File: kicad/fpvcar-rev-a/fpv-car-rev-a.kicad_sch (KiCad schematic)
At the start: 13 parts, among them J1 CAMERA, U1 ESP32-S3-WROOM-1, U2 AMS1117-3.3

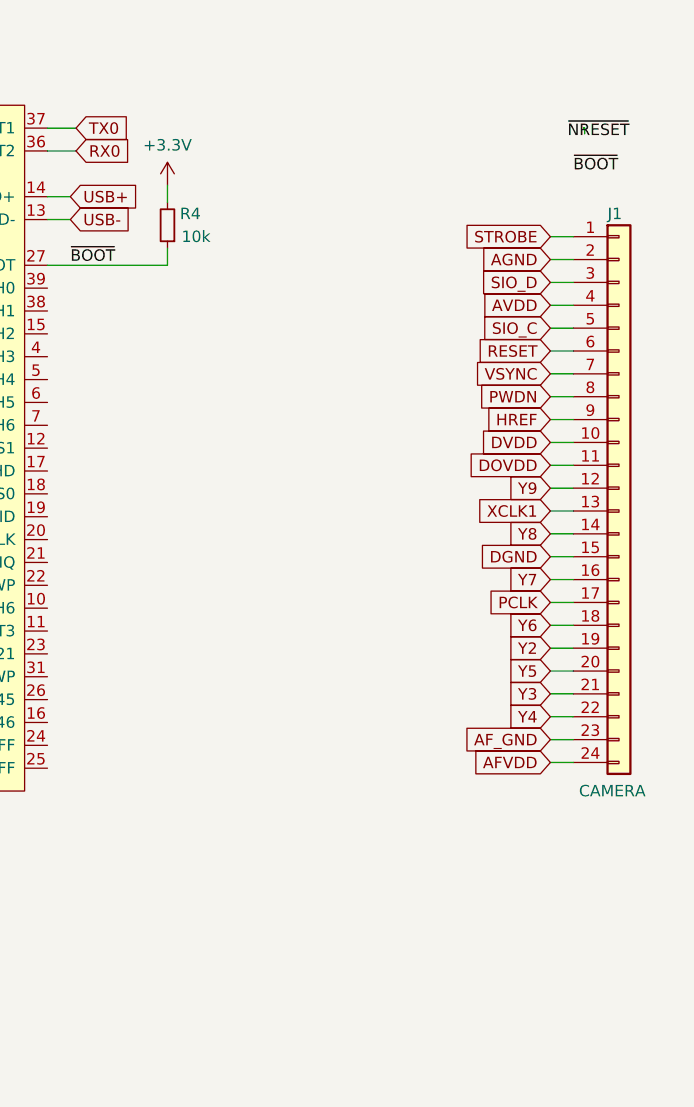
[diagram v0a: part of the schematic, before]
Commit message: Initial testcode (for esp32cam) and some more improvements on schematic
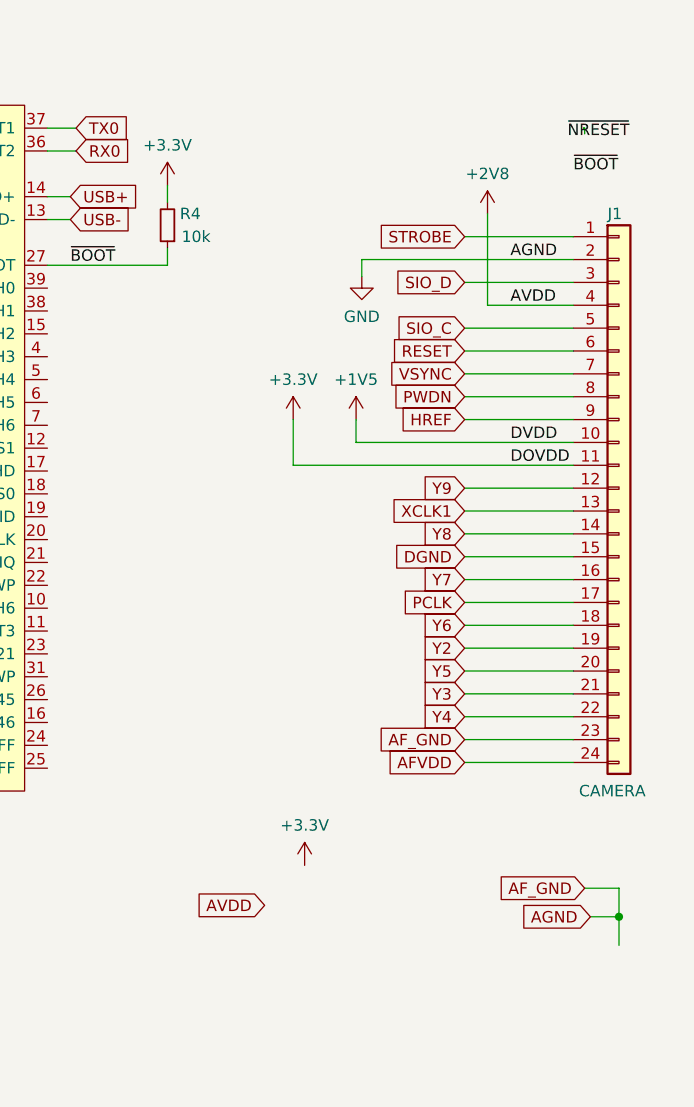
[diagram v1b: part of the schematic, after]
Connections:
- net AF_GND is gone; now on net GND: J1.23 (Pin_23)
- net AGND is gone; now on net GND: J1.2 (Pin_2)
- net DOVDD is gone; now on net +3.3V: J1.11 (Pin_11)
- net AVDD renamed +2V8
- net DVDD renamed +1V5

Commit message: Schematic progress!
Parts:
- added C10, C9: 47u, Capacitor_SMD:C_Elec_4x5.4, symbol Device:C_Small
- added C11: 2.2u, Capacitor_SMD:C_0402_1005Metric, symbol Device:C_Small
- added C12: 10n, Capacitor_SMD:C_0402_1005Metric, symbol Device:C_Small
- added C5, C6, C7, C8: 10u, symbol Device:C_Small
- added J2: Steering, symbol Connector_Generic:Conn_01x03
- added J3: RGB Leds, symbol Connector_Generic:Conn_01x03
- added J4: Battery, symbol Connector_Generic:Conn_01x02
- added J5: Debug UART, symbol Connector_Generic:Conn_01x03
- added J6, J7: M1, symbol Connector_Generic:Conn_01x02
- added J8: NRF24L01, Connector_PinSocket_2.54mm:PinSocket_1x08_P2.54mm_Vertical, symbol Connector_Generic:Conn_01x08
- added OSC1: YF4024M00033001, easyeda2kicad:OSC-SMD_4P-L3.2-W2.5-BL_1C210000BB0F, symbol easyeda2kicad:YF4024M00033001
- added R5: 10k, symbol Device:R_Small
- added SW1, SW2: SW_SPST, symbol Switch:SW_SPST
- added TP1: TestPoint, symbol Connector:TestPoint
- added U3: TLV74328PDBVR, easyeda2kicad:SOT-23-5_L3.0-W1.7-P0.95-LS2.8-BL, symbol easyeda2kicad:TLV74328PDBVR
- added U4: TLV74315PDBVR, easyeda2kicad:SOT-23-5_L2.9-W1.6-P0.95-LS2.8-BL, symbol easyeda2kicad:TLV74315PDBVR
- added U5: DRV8833PWP, Package_SO:HTSSOP-16-1EP_4.4x5mm_P0.65mm_EP3.4x5mm_Mask2.46x2.31mm_ThermalVias, symbol Driver_Motor:DRV8833PWP
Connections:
- net +1V5: now also C8.1, U4.5 (OUT)
- net +2V8: now also C5.1, U3.5 (OUT)
- net +3.3V: now also C10.1, J8.1 (Pin_1), OSC1.4 (VDD)
- net GND: now also C10.2, C11.1, C5.2, C6.2, C7.2, C8.2, C9.2, J2.3 (Pin_3), J3.3 (Pin_3), J4.2 (Pin_2), J5.3 (Pin_3), J8.2 (Pin_2), OSC1.2 (GND), SW1.2 (B), SW2.2 (B), U3.2 (GND), U4.2 (GND), U5.13 (GND), U5.17 (GND(PPAD)), U5.3 (AISEN), U5.6 (BISEN); no longer J1.23 (Pin_23)
- net RX0: now also J5.2 (Pin_2)
- net TX0: now also J5.1 (Pin_1)
- net VBUS: now also C6.1, C7.1, U3.1 (IN), U3.3 (EN), U4.1 (IN), U4.3 (EN)
- net XCLK1: now also OSC1.3 (OUT)
- net ~{BOOT}: now also SW1.1 (A)
- net ~{NRESET}: now also SW2.1 (A)
- new net: R5.2, U5.1 (nSLEEP)
- new net: C12.2, U5.11 (VCP)
- new net: C11.2, U5.14 (VINT)
- new net +5V: J2.2 (Pin_2), J3.2 (Pin_2)
- new net AF_GND: J1.23 (Pin_23)
- new net MOTOR_1_IN: J6.1 (Pin_1), U5.2 (AOUT1)
- new net MOTOR_1_OUT: J6.2 (Pin_2), U5.4 (AOUT2)
- new net MOTOR_2_IN: J7.1 (Pin_1), U5.7 (BOUT1)
- new net MOTOR_2_OUT: J7.2 (Pin_2), U5.5 (BOUT2)
- new net MOTOR_A_IN1: U5.16 (AIN1)
- new net MOTOR_A_IN2: U5.15 (AIN2)
- new net MOTOR_B_IN1: U5.9 (BIN1)
- new net MOTOR_B_IN2: U5.10 (BIN2)
- new net NRF_CE: J8.3 (Pin_3)
- new net NRF_CSN: J8.4 (Pin_4)
- new net NRF_IRQ: J8.8 (Pin_8)
- new net NRF_MISO: J8.7 (Pin_7)
- new net NRF_MOSI: J8.6 (Pin_6)
- new net NRF_SCK: J8.5 (Pin_5)
- new net RGB_LED: J3.1 (Pin_1)
- new net STEER: J2.1 (Pin_1)
- new net VBAT: J4.1 (Pin_1)
- new net VCC: C12.1, C9.1, R5.1, U5.12 (VM)
- new net ~{MOTOR_NFAULT}: TP1.1, U5.8 (nFAULT)
- no-connect marks 0 -> 3
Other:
- note added: "Buttons"
- note added: "Camera (OV5640)"
- note added: "Connectors"
- note added: "LEDs"
- note added: "MCU"
- note added: "Motor driver (H-bridge)"
- note added: "NRF24L01 Radio (smd module)"
- note added: "Oscillator for camera"
- note added: "Power supplies"
- moved on the sheet: C1, C2, C3, C4, D1, D2, J1, R1, R2, R3, R4, U1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

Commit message: More schematic improvements
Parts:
- removed OSC1: YF4024M00033001, easyeda2kicad:OSC-SMD_4P-L3.2-W2.5-BL_1C210000BB0F, symbol easyeda2kicad:YF4024M00033001
- added J10, J9: GPIO, symbol Connector_Generic:Conn_01x04
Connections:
- net +3.3V: now also J10.3 (Pin_3)
- net +5V: now also J9.3 (Pin_3)
- net GND: now also J10.4 (Pin_4), J9.4 (Pin_4)
- net RESET renamed ~{RESET}
- new net GPIO00: J10.1 (Pin_1), J10.2 (Pin_2), J9.1 (Pin_1), J9.2 (Pin_2)
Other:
- note added: "- RESET: Active low, internal pull-up - PWDN (Power down): Active high, internal pull-down"
- note added: "Pinouts - SIOC - SCCB Input clock - SIOD - SCCB Data - XCLK1 - System input clock - VSYNC - DVP VSYNC output - HREF - DVP HREF output Input clock to camera is driven by GPIOs on ESP"
- note removed: "Oscillator for camera"
- moved on the sheet: C1, C11, C12, C2, C5, C6, C7, C8, C9, D1, D2, R1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

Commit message: Swapped to OV2640 camera, started layout
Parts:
- removed C7, C8: 10u, symbol Device:C_Small
- removed J3: RGB Leds, symbol Connector_Generic:Conn_01x03
- removed U2: AMS1117-3.3, Package_TO_SOT_SMD:SOT-223-3_TabPin2, symbol Regulator_Linear:AMS1117-3.3
- removed U3: TLV74328PDBVR, easyeda2kicad:SOT-23-5_L3.0-W1.7-P0.95-LS2.8-BL, symbol easyeda2kicad:TLV74328PDBVR
- removed U4: TLV74315PDBVR, easyeda2kicad:SOT-23-5_L2.9-W1.6-P0.95-LS2.8-BL, symbol easyeda2kicad:TLV74315PDBVR
- added C13: 0.1u, Capacitor_SMD:C_0402_1005Metric, symbol Device:C_Small
- added C14, C15, C18, C19: 10u, Capacitor_SMD:C_0603_1608Metric, symbol Device:C_Small
- added D3: D_Schottky, Diode_SMD:D_SOD-123, symbol Device:D_Schottky
- added D4: Schottky, Diode_SMD:D_SOD-123, symbol Device:D_Schottky
- added H1, H2, H3, H4: MountingHole_Pad, symbol Mechanical:MountingHole_Pad
- added J11: USB C, easyeda2kicad:USB-SMD_GT-USB-7010AN, symbol Connector:USB_C_Receptacle_USB2.0
- added J12, J13: GPIO, Connector_PinSocket_2.54mm:PinSocket_1x04_P2.54mm_Vertical, symbol Connector_Generic:Conn_01x04
- added J14: RGB FL, Connector_PinSocket_2.00mm:PinSocket_1x04_P2.00mm_Vertical, symbol Connector_Generic:Conn_01x04
- added J15: RGB FR, Connector_PinSocket_2.00mm:PinSocket_1x04_P2.00mm_Vertical, symbol Connector_Generic:Conn_01x04
- added J16: RGB BL, Connector_PinSocket_2.00mm:PinSocket_1x04_P2.00mm_Vertical, symbol Connector_Generic:Conn_01x04
- added J17: RGB BR, Connector_PinSocket_2.00mm:PinSocket_1x04_P2.00mm_Vertical, symbol Connector_Generic:Conn_01x04
- added Q1: Q_PMOS_GSD, Package_TO_SOT_SMD:SOT-23, symbol Device:Q_PMOS_GSD
- added R10: 10k, Resistor_SMD:R_0402_1005Metric, symbol Device:R
- added R11, R13, R6, R7: 10k, Resistor_SMD:R_0402_1005Metric, symbol Device:R_Small
- added R12, R14: 4.7k, Resistor_SMD:R_0402_1005Metric, symbol Device:R_Small
- added R8, R9: 5.11k, Resistor_SMD:R_0402_1005Metric, symbol Device:R
- added U2: AMS1117-5.0, Package_TO_SOT_SMD:SOT-223-3_TabPin2, symbol Regulator_Linear:AMS1117-5.0
- added U3: XC6206-1.2V, Package_TO_SOT_SMD:SOT-23-3, symbol Regulator_Linear:XC6206PxxxMR
- added U4: XC6206-2.8V, Package_TO_SOT_SMD:SOT-23-3, symbol Regulator_Linear:XC6206PxxxMR
- added U6: WL2803K33-5/TR, Package_TO_SOT_SMD:SOT-89-5, symbol easyeda2kicad:WL2803K33-5_TR
- C1, C2, C3, C5, C6: footprint (none) -> Capacitor_SMD:C_0603_1608Metric
- C10, C9: footprint Capacitor_SMD:C_Elec_4x5.4 -> Capacitor_SMD:C_1206_3216Metric
- C4: footprint (none) -> Capacitor_SMD:C_0402_1005Metric
- D1, D2: footprint (none) -> LED_SMD:LED_0603_1608Metric
- J10, J9: footprint (none) -> Connector_PinSocket_2.54mm:PinSocket_1x04_P2.54mm_Vertical
- J2, J5: footprint (none) -> Connector_PinSocket_2.54mm:PinSocket_1x03_P2.54mm_Vertical
- J4, J6: footprint (none) -> Connector_PinSocket_2.54mm:PinSocket_1x02_P2.54mm_Vertical
- J7: value M1 -> M2; footprint (none) -> Connector_PinSocket_2.54mm:PinSocket_1x02_P2.54mm_Vertical
- J8: footprint Connector_PinSocket_2.54mm:PinSocket_1x08_P2.54mm_Vertical -> Connector_PinHeader_1.27mm:PinHeader_1x08_P1.27mm_Vertical
- R1, R2, R3, R4, R5: footprint (none) -> Resistor_SMD:R_0402_1005Metric
- SW1, SW2: footprint (none) -> easyeda2kicad:SW-SMD_L4.0-W2.9-LS5.0
- U1: footprint PCM_Espressif:ESP32-S3-WROOM-1 -> Espressif:ESP32-S3-WROOM-1
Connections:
- net +1V5 is gone; now on net GND: J1.10 (Pin_10)
- net AFVDD is gone; now on net STROBE: J1.24 (Pin_24)
- net AF_GND is gone; now on net GND: J1.23 (Pin_23)
- net SIO_C is gone; now on net DATA5: J1.5 (Pin_5)
- net SIO_D is gone; now on net DATA4: J1.3 (Pin_3)
- net XCLK1 is gone; now on net DATA9: J1.13 (Pin_13)
- net Y2 is gone; now on net ~{RESET}: J1.19 (Pin_19)
- net Y3 is gone; now on net +2V8: J1.21 (Pin_21)
- net Y4 is gone; now on net SIOD: J1.22 (Pin_22)
- net Y5 is gone; now on net SIOC: J1.20 (Pin_20)
- net Y6 is gone; now on net VSYNC: J1.18 (Pin_18)
- net Y7 is gone; now on net HREF: J1.16 (Pin_16)
- net Y8 is gone; now on net +3.3V: J1.14 (Pin_14)
- net +2V8: now also C6.1, U4.2 (VO); no longer C5.1, J1.4 (Pin_4)
- net +3.3V: now also C12.1, C5.1, R5.1, C13.1, C15.1, C18.1, J12.3 (Pin_3), J13.3 (Pin_3), R6.2, U3.3 (VI), U4.3 (VI), U6.5 (VOUT); no longer C1.1, J1.11 (Pin_11)
- net +5V: now also C1.1, J14.3 (Pin_3), J15.3 (Pin_3), J16.3 (Pin_3), J17.3 (Pin_3), U2.2 (VO)
- net GND: now also C13.2, C14.2, C15.2, C18.2, C19.2, H1.1, H2.1, H3.1, H4.1, J11.A1 (GND), J11.A12 (GND), J11.B1 (GND), J11.B12 (GND), J11.S1 (SHIELD), J12.4 (Pin_4), J13.4 (Pin_4), J14.4 (Pin_4), J15.4 (Pin_4), J16.4 (Pin_4), J17.4 (Pin_4), R10.2, R12.2, R14.2, R7.1, R8.2, R9.2, U2.1 (GND), U3.1 (GND), U4.1 (GND), U6.2 (GND); no longer J1.2 (Pin_2)
- net GPIO00: now also J12.1 (Pin_1), J12.2 (Pin_2), J13.1 (Pin_1), J13.2 (Pin_2)
- net HREF: no longer J1.9 (Pin_9)
- net PCLK: now also J1.8 (Pin_8); no longer J1.17 (Pin_17)
- net PWDN: now also J1.17 (Pin_17), R7.2; no longer J1.8 (Pin_8)
- net RGB_LED: now also J14.1 (Pin_1)
- net STROBE: no longer J1.1 (Pin_1)
- net USB+: now also J11.A6 (D+), J11.B6 (D+)
- net USB-: now also J11.A7 (D-), J11.B7 (D-)
- net VBAT: now also C2.1, C9.1, U5.12 (VM), D4.2 (A), R11.1, U2.3 (VI)
- net VBUS: now also D3.2 (A), J11.A4 (VBUS), J11.A9 (VBUS), J11.B4 (VBUS), J11.B9 (VBUS), Q1.1 (G), R10.1, R13.1; no longer C2.1, C6.1
- net VSYNC: no longer J1.7 (Pin_7)
- net ~{RESET}: now also R6.1; no longer J1.6 (Pin_6)
- net DATA0: now reaches U1.15 (GPIO3/TOUCH3/ADC1_CH2)
- net DATA0: now also J1.1 (Pin_1)
- net DATA1: now reaches U1.16 (GPIO46)
- net DATA1: now also J1.2 (Pin_2)
- net DATA4: now reaches U1.17 (GPIO9/TOUCH9/ADC1_CH8/FSPIHD/SUBSPIHD)
- net DATA3: now reaches U1.18 (GPIO10/TOUCH10/ADC1_CH9/FSPICS0/FSPIIO4/SUBSPICS0)
- net DATA3: now also J1.4 (Pin_4)
- net DATA5: now reaches U1.19 (GPIO11/TOUCH11/ADC2_CH0/FSPID/FSPIIO5/SUBSPID)
- net DATA2: now reaches U1.20 (GPIO12/TOUCH12/ADC2_CH1/FSPICLK/FSPIIO6/SUBSPICLK)
- net DATA2: now also J1.6 (Pin_6)
- net DATA6: now reaches U1.21 (GPIO13/TOUCH13/ADC2_CH2/FSPIQ/FSPIIO7/SUBSPIQ)
- net DATA6: now also J1.7 (Pin_7)
- net DATA7: now reaches U1.22 (GPIO14/TOUCH14/ADC2_CH3/FSPIWP/FSPIDQS/SUBSPIWP)
- net DATA7: now also J1.9 (Pin_9)
- net DATA8: now reaches U1.23 (GPIO21)
- net DATA8: now also J1.11 (Pin_11)
- net DATA9: now reaches U1.24 (GPIO47/SPICLK_P/SUBSPICLK_P_DIFF)
- net SIOC: now reaches U1.25 (GPIO48/SPICLK_N/SUBSPICLK_N_DIFF)
- net SIOD: now reaches U1.26 (GPIO45)
- net DGND renamed +1V2
- net +1V2: now also C19.1, U3.2 (VO)
- net MOTOR_1_IN renamed MOTOR_A_OUT1
- net MOTOR_1_OUT renamed MOTOR_A_OUT2
- net MOTOR_2_IN renamed MOTOR_B_OUT1
- net MOTOR_2_OUT renamed MOTOR_B_OUT2
- removed net VCC: C12.1, C9.1, R5.1, U5.12 (VM)
- net Y9 renamed XCLK
- new net: J11.A5 (CC1), R9.1
- new net: J11.B5 (CC2), R8.1
- new net: D4.1 (K), Q1.3 (D)
- new net BATT_VOLTAGE: R11.2, R12.1
- new net RGB_BL_BR: J16.2 (Pin_2), J17.1 (Pin_1)
- new net RGB_FL_FR: J14.2 (Pin_2), J15.1 (Pin_1)
- new net RGB_FR_BL: J15.2 (Pin_2), J16.1 (Pin_1)
- new net USB_SENSE: R13.2, R14.1
- new net VSYS: C14.1, D3.1 (K), Q1.2 (S), U6.1 (VIN), U6.3 (EN)
- no-connect marks 3 -> 5
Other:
- note added: "2.8V and 1.2V are for the camera"
- note added: "5V LDO is connected straight to battery, and requires 2s battery to output 5V"
- note added: "CC pins pulled down with 5.11k resistors should give 5V & 3A."
- note added: "Camera (OV2640)"
- note added: "Input voltage options: - 2s - 1s -> Note that 5V LDOs will NOT work if 1s is supplied"
- note added: "Mounting holes"
- note added: "Notes: Pins are reversed (1-24) due to footprint - RESET: Active low, internal pull-up - PWDN (Power down): Active high, internal pull-down, So R6 and R7 are probably NOT needed - SIOC - SCCB Input clock - SIOD - SCCB Data - XCLK - System input clock - VSYNC - DVP VSYNC output - HREF - DVP HREF output - DATA0-9 - Data pins Voltages: - DVDD: 1.2V - DOVDD: 3.3V - AVVD: 2.8V"
- note added: "USB connected: 1) VBAT > VUSB: PMOS open (Battery power) 2) VBAT < USB: PMOS close (USB power) USB not connected: PMOS open (Battery power)"
- note added: "Voltage measurement & USB detect"
- note removed: "- RESET: Active low, internal pull-up - PWDN (Power down): Active high, internal pull-down"
- note removed: "Camera (OV5640)"
- note removed: "Pinouts - SIOC - SCCB Input clock - SIOD - SCCB Data - XCLK1 - System input clock - VSYNC - DVP VSYNC output - HREF - DVP HREF output Input clock to camera is driven by GPIOs on ESP"
- moved on the sheet: C1, C10, C11, C12, C2, C9, D1, D2, J1, J10, J2, J4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

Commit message: PCB for rev. A done!
PCB name: S3Voyager :)
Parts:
- removed J10, J13: GPIO, Connector_PinSocket_2.54mm:PinSocket_1x04_P2.54mm_Vertical, symbol Connector_Generic:Conn_01x04
- removed TP1: TestPoint, symbol Connector:TestPoint
- added J3: Bat Power, Custom3:conn_01x04, symbol Connector_Generic:Conn_01x04
- H1, H2, H3, H4: footprint (none) -> MountingHole:MountingHole_2.2mm_M2_Pad_Via
- J12: value GPIO -> 3.3V Power; footprint Connector_PinSocket_2.54mm:PinSocket_1x04_P2.54mm_Vertical -> Custom3:conn_01x04
- J14, J15, J16, J17: footprint Connector_PinSocket_2.00mm:PinSocket_1x04_P2.00mm_Vertical -> Custom3:RGB_4_Pin_2mm_Female
- J9: value GPIO -> 5V Power; footprint Connector_PinSocket_2.54mm:PinSocket_1x04_P2.54mm_Vertical -> Custom3:conn_01x04
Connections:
- net +3.3V: now also J12.1 (Pin_1), J12.2 (Pin_2); no longer J12.3 (Pin_3)
- net +5V: now also J9.1 (Pin_1), J9.2 (Pin_2); no longer J9.3 (Pin_3)
- net BATT_VOLTAGE: now also U1.38 (GPIO2/TOUCH2/ADC1_CH1)
- net DATA1: now also U1.12 (GPIO8/TOUCH8/ADC1_CH7/SUBSPICS1); no longer U1.16 (GPIO46)
- net GND: now also J12.3 (Pin_3), J9.3 (Pin_3), J3.3 (Pin_3), J3.4 (Pin_4)
- net HREF: now also U1.30 (SPIDQS/GPIO37/FSPIQ/SUBSPIQ)
- net LED_BLUE: now also U1.16 (GPIO46)
- net LED_RED: now also U1.6 (GPIO6/TOUCH6/ADC1_CH5)
- net MOTOR_A_IN1: now also U1.7 (GPIO7/TOUCH7/ADC1_CH6)
- net MOTOR_A_IN2: now also U1.8 (GPIO15/U0RTS/ADC2_CH4/XTAL_32K_P)
- net MOTOR_A_OUT1: now also J7.1 (Pin_1); no longer J6.1 (Pin_1)
- net MOTOR_A_OUT2: now also J7.2 (Pin_2); no longer J6.2 (Pin_2)
- net MOTOR_B_IN1: now also U1.32 (MTCK/GPIO39/CLK_OUT3/SUBSPICS1)
- net MOTOR_B_IN2: now also U1.31 (GPIO38/FSPIWP/SUBSPIWP)
- net MOTOR_B_OUT1: now also J6.1 (Pin_1); no longer J7.1 (Pin_1)
- net MOTOR_B_OUT2: now also J6.2 (Pin_2); no longer J7.2 (Pin_2)
- net NRF_CE: now also U1.4 (GPIO4/TOUCH4/ADC1_CH3)
- net NRF_CSN: now also U1.5 (GPIO5/TOUCH5/ADC1_CH4)
- net NRF_MISO: now also U1.33 (MTDO/GPIO40/CLK_OUT2)
- net NRF_MOSI: now also U1.34 (MTDI/GPIO41/CLK_OUT1)
- net NRF_SCK: now also U1.35 (MTMS/GPIO42)
- net PCLK: now also U1.11 (GPIO18/U1RXD/ADC2_CH7/CLK_OUT3)
- net RGB_BL_BR: now also J16.1 (Pin_1), J17.2 (Pin_2); no longer J16.2 (Pin_2), J17.1 (Pin_1)
- net RGB_FR_BL: now also J17.1 (Pin_1); no longer J16.1 (Pin_1)
- net RGB_LED: now also U1.28 (SPIIO6/GPIO35/FSPID/SUBSPID)
- net STEER: now also U1.9 (GPIO16/U0CTS/ADC2_CH5/XTAL_32K_N)
- net USB_SENSE: now also U1.39 (GPIO1/TOUCH1/ADC1_CH0)
- net VBAT: now also J3.1 (Pin_1), J3.2 (Pin_2)
- net VSYNC: now also U1.29 (SPIIO7/GPIO36/FSPICLK/SUBSPICLK)
- net XCLK: now also U1.10 (GPIO17/U1TXD/ADC2_CH6)
- removed net GPIO00: J12.1 (Pin_1), J12.2 (Pin_2), J9.1 (Pin_1), J9.2 (Pin_2)
- no-connect marks 5 -> 7
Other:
- note added: "GPIO0 & GPIO46 are strapping pins. Needs to be 0 on boot to flash"
- company: (none) -> Victor Krook
- title: (none) -> S3Voyager
- moved on the sheet: C11, C12, C3, C4, C9, H1, H2, H3, H4, J12, J14, J15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
